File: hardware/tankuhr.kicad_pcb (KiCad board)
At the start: 2 copper layers, 50 x 50 mm, 30 parts, among them J1 Conn_01x04_Pin, J2 Conn_01x04_Pin, J3 Conn_01x04_Pin, U1 TBA1-1211, U2 XIAO-ESP32-C3-SMD

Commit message: start with r2 hardware
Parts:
- added D2: 1N5817, Diode_THT:D_DO-41_SOD81_P7.62mm_Horizontal, F.Cu at (59.0, 83.3)
- added D3: LED, LED_SMD:LED_PLCC-2_3.4x3.0mm_AK, F.Cu at (51.8, 71.2)
- added F1: 1A, Fuse:Fuse_1206_3216Metric, F.Cu at (55.5, 81.2)
- added JP1: SolderJumper_2_Bridged, Jumper:SolderJumper-2_P1.3mm_Bridged2Bar_Pad1.0x1.5mm, F.Cu at (95.8, 88.6)
- C3, C4, C5, C6, R6, R7: footprint Capacitor_SMD:C_0805_2012Metric -> Capacitor_SMD:C_0805_2012Metric_Pad1.18x1.45mm_HandSolder
- J1, J2, J3: footprint Connector_PinHeader_2.54mm:PinHeader_1x04_P2.54mm_Vertical -> Connector_JST:JST_GH_BM04B-GHS-TBT_1x04-1MP_P1.25mm_Vertical
- R1, R2, R3, R5: footprint Resistor_SMD:R_0805_2012Metric -> Resistor_SMD:R_0805_2012Metric_Pad1.20x1.40mm_HandSolder
- R4: value 0 -> ?; footprint Connector_PinHeader_2.54mm:PinHeader_1x02_P2.54mm_Vertical -> Resistor_SMD:R_0805_2012Metric_Pad1.20x1.40mm_HandSolder
- TP1, TP2, TP3, TP4: footprint TestPoint:TestPoint_THTPad_2.0x2.0mm_Drill1.0mm -> TestPoint:TestPoint_Pad_D1.0mm
- moved R4 39.6 mm to (56.6, 71.2)
- moved L1 4.94 mm to (61.9, 83.2)
- moved L2 4.94 mm to (61.9, 87.0)
- moved C2 4.69 mm to (81.2, 83.5)
- moved C3 4.69 mm to (74.8, 85.0)
- moved J1 3.98 mm to (50.8, 84.9), turned to 90 degrees
- moved J2 3.87 mm to (51.0, 63.1), turned to 90 degrees
- moved U1 3.69 mm to (91.7, 89.3)
- moved TP4 3.45 mm to (95.5, 81.8), turned to 0 degrees
- moved J3 2.85 mm to (94.0, 62.0), turned to -90 degrees
- moved TP1 2.54 mm to (56.0, 66.5)
- moved C5 1.83 mm to (58.9, 64.0)
- moved R5 1.83 mm to (58.9, 66.5)
- moved TP2 1.82 mm to (54.2, 57.8)
- moved C6 1.60 mm to (86.5, 57.5)
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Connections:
- C2 pad 2: Net-(U1--Vin) -> Net-(JP1-A)
- C3 pad 2: Net-(U1--Vin) -> Net-(JP1-A)
- J1 pad 1: +12V -> GNDA
- J1 pad 2: +12V -> GNDA
- J1 pad 3: GNDA -> Net-(J1-Pin_3)
- J1 pad 4: GNDA -> Net-(J1-Pin_3)
- J2 pad 1: SENSOR_FUEL_LEVEL -> SENSOR_FUEL_FLOW
- J2 pad 4: SENSOR_FUEL_FLOW -> SENSOR_FUEL_LEVEL
- L2 pad 2: Net-(U1--Vin) -> Net-(JP1-A)
- R4 pad 1: Net-(U1--Vin) -> USER_LED0
- R4 pad 2: GND -> Net-(D3-A)
- U1 pad 1: Net-(U1--Vin) -> Net-(JP1-A)
- U2 pad 4: unconnected-(U2-GPIO5_A3_D3-Pad4) -> USER_LED0
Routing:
- net Net-(U1--Vin): track 27.5 -> 0.00 mm
- net Net-(JP1-A): track 0.00 -> 26.0 mm
- net USER_LED0: track 0.00 -> 15.3 mm
- net GND: track 16.3 -> 29.0 mm, vias 15 -> 14
- net +12V: track 15.6 -> 2.99 mm
- net Net-(D2-A): track 0.00 -> 5.61 mm
- net GNDA: track 15.6 -> 10.5 mm
- net Net-(J3-Pin_1): track 33.5 -> 37.9 mm, vias 2 -> 0
- net +5V: track 4.30 -> 0.00 mm
- net Net-(J1-Pin_3): track 0.00 -> 4.14 mm
- net Net-(D3-A): track 0.00 -> 2.42 mm
- net SENSOR_FUEL_LEVEL: track 10.1 -> 8.44 mm
- net +3.3V: track 12.6 -> 11.0 mm
- net Net-(J3-Pin_4): track 33.4 -> 35.0 mm, vias 2 -> 0
- net Net-(U2-GPIO3_A1_D1): track 14.7 -> 16.2 mm
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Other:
- board text added: "Tankuhr r2"
- board text removed: "Tankuhr r1"

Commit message: WIP
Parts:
- removed D2: 1N5817, Diode_THT:D_DO-41_SOD81_P7.62mm_Horizontal
- removed D3: LED, LED_SMD:LED_PLCC-2_3.4x3.0mm_AK
- removed L2: 2uH, Inductor_THT:L_Axial_L7.0mm_D3.3mm_P10.16mm_Horizontal_Fastron_MICC
- removed R3: 390, Resistor_SMD:R_0805_2012Metric_Pad1.20x1.40mm_HandSolder
- removed R4: ?, Resistor_SMD:R_0805_2012Metric_Pad1.20x1.40mm_HandSolder
- added R10: 220, Resistor_SMD:R_0805_2012Metric_Pad1.20x1.40mm_HandSolder, F.Cu at (68.9, 103.8)
- added R11: 0, Resistor_SMD:R_0805_2012Metric_Pad1.20x1.40mm_HandSolder, F.Cu at (68.9, 106.8)
- added R8: 4.7k, Resistor_SMD:R_0805_2012Metric_Pad1.20x1.40mm_HandSolder, F.Cu at (83.0, 106.0)
- added R9: 100, Resistor_SMD:R_0805_2012Metric_Pad1.20x1.40mm_HandSolder, F.Cu at (68.9, 100.9)
- added U3: MCP6002-xMC, Package_DFN_QFN:DFN-8-1EP_3x2mm_P0.5mm_EP1.75x1.45mm, F.Cu at (74.0, 100.0)
- C1: value 22u / 10V -> 1n; footprint Capacitor_THT:CP_Radial_D4.0mm_P1.50mm -> Capacitor_SMD:C_0805_2012Metric_Pad1.18x1.45mm_HandSolder
- C2: value 100u / 35V -> 4.7u; footprint Capacitor_THT:CP_Radial_D8.0mm_P3.50mm -> Capacitor_THT:CP_Radial_D5.0mm_P2.00mm
- C3: value 100n / >35V -> 10u; footprint Capacitor_SMD:C_0805_2012Metric_Pad1.18x1.45mm_HandSolder -> Capacitor_THT:CP_Radial_D5.0mm_P2.00mm
- C5: value 100n -> 1n
- D1: value LED -> BAT54W; footprint LED_SMD:LED_PLCC-2_3.4x3.0mm_AK -> Package_TO_SOT_SMD:SOT-323_SC-70
- L1: value 2uH -> L; footprint Inductor_THT:L_Axial_L7.0mm_D3.3mm_P10.16mm_Horizontal_Fastron_MICC -> asdf:RECOM RLS-126
- R1: value 220 -> 3.3k / 330
- R2: value 6.8k -> 1k
- R5: value 330 -> 220
- R6, R7: footprint Capacitor_SMD:C_0805_2012Metric_Pad1.18x1.45mm_HandSolder -> Resistor_SMD:R_0805_2012Metric_Pad1.20x1.40mm_HandSolder
- U1: value TBA1-1211 -> R-78E5.0-0.5; footprint Converter_DCDC:Converter_DCDC_TRACO_TBA1-xxxx_THT -> Converter_DCDC:Converter_DCDC_RECOM_R-78E-0.5_THT
- moved U2 50.5 mm to (123.0, 59.6)
- moved D1 43.9 mm to (57.0, 81.3), turned to 0 degrees
- moved U1 15.9 mm to (77.3, 82.6), turned to -90 degrees
- moved C3 14.3 mm to (60.5, 86.0)
- moved C2 12.0 mm to (69.5, 86.0)
- moved TP4 9.74 mm to (87.0, 86.5)
- moved JP1 8.95 mm to (86.8, 89.5), turned to 0 degrees
- moved TP2 4.43 mm to (50.0, 56.5)
- moved TP1 3.91 mm to (53.0, 69.0)
- moved F1 3.58 mm to (54.0, 78.0), turned to 0 degrees
- moved L1 2.15 mm to (62.0, 81.0)
- moved R1 1.17 mm to (54.0, 56.0)
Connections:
- net Net-(J3-Pin_1) renamed SDA
- net Net-(J3-Pin_4) renamed SCL
- net Net-(U2-GPIO3_A1_D1) renamed D1
- C1 pad 1: Net-(U2-GPIO2_A0_D0) -> D0
- C2 pad 1: Net-(U1-+Vin) -> Net-(U1-IN)
- C2 pad 2: Net-(JP1-A) -> GNDA
- C3 pad 1: Net-(U1-+Vin) -> +12V
- C3 pad 2: Net-(JP1-A) -> GNDA
- D1 pad 1: GND -> Net-(D1-A)
- D1 pad 2: Net-(D1-A) -> unconnected-(D1-NC-Pad2)
- F1 pad 2: Net-(D2-A) -> Net-(D1-A)
- J3 pad 2: GND -> +3.3V
- JP1 pad 1: Net-(JP1-A) -> GNDA
- L1 pad 2: Net-(U1-+Vin) -> Net-(U1-IN)
- R1 pad 2: +5V -> +3.3V
- R2 pad 1: SENSOR_FUEL_LEVEL -> Net-(R10-Pad1)
- R2 pad 2: Net-(U2-GPIO2_A0_D0) -> Net-(U3A--)
- U1 pad 1: Net-(JP1-A) -> Net-(U1-IN)
- U1 pad 2: Net-(U1-+Vin) -> GNDA
- U1 pad 3: GND -> +5V
- U2 pad 1: Net-(U2-GPIO2_A0_D0) -> D0
- U2 pad 4: USER_LED0 -> unconnected-(U2-GPIO5_A3_D3-Pad4)
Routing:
- net SDA: track 37.9 -> 0.00 mm
- net SCL: track 35.0 -> 0.00 mm
- net GND: track 29.0 -> 0.00 mm, vias 14 -> 0
- net Net-(JP1-A): track 26.0 -> 0.00 mm
- net Net-(U1-+Vin): track 21.6 -> 0.00 mm
- net D1: track 16.2 -> 0.00 mm
- net USER_LED0: track 15.3 -> 0.00 mm
- net +3.3V: track 11.0 -> 0.00 mm
- net GNDA: track 10.5 -> 0.00 mm
- net Net-(U2-GPIO2_A0_D0): track 9.41 -> 0.00 mm
- net SENSOR_FUEL_LEVEL: track 8.44 -> 0.00 mm
- net SENSOR_FUEL_FLOW: track 5.67 -> 0.00 mm
- net Net-(D2-A): track 5.61 -> 0.00 mm
- net Net-(J1-Pin_3): track 4.14 -> 0.00 mm
- net Net-(D1-A): track 3.13 -> 0.00 mm
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- removed copper zone on F.Cu, net +5V
- removed copper zone on B.Cu, net GND
- removed copper zone on F.Cu, net GND

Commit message: complete r2 hardware
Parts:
- removed U3: MCP6002-xMC, Package_DFN_QFN:DFN-8-1EP_3x2mm_P0.5mm_EP1.75x1.45mm
- added D2: LED, LED_SMD:LED_0805_2012Metric_Pad1.15x1.40mm_HandSolder, F.Cu at (70.5, 71.5)
- added D3: LED, LED_SMD:LED_0805_2012Metric_Pad1.15x1.40mm_HandSolder, F.Cu at (73.0, 71.5)
- added D4: LED, LED_SMD:LED_0805_2012Metric_Pad1.15x1.40mm_HandSolder, F.Cu at (68.0, 71.5)
- added J4: Micro_SD_Card_Det1, Connector_Card:microSD_HC_Molex_104031-0811, F.Cu at (90.5, 65.1)
- added R12: 150, Resistor_SMD:R_0805_2012Metric_Pad1.20x1.40mm_HandSolder, F.Cu at (68.0, 75.5)
- added R3: 150, Resistor_SMD:R_0805_2012Metric_Pad1.20x1.40mm_HandSolder, F.Cu at (70.5, 75.5)
- added R4: 150, Resistor_SMD:R_0805_2012Metric_Pad1.20x1.40mm_HandSolder, F.Cu at (73.0, 75.5)
- added U5: MCP6001-OT, Package_TO_SOT_SMD:SOT-23-5, F.Cu at (57.5, 63.1)
- L1: footprint asdf:RECOM RLS-126 -> Library:RECOM RLS-120
- moved R10 49.2 mm to (59.5, 55.5), turned to 90 degrees
- moved U2 49.0 mm to (74.0, 58.5)
- moved R11 48.9 mm to (58.5, 59.0)
- moved R8 46.7 mm to (56.5, 67.5), turned to 90 degrees
- moved R9 39.0 mm to (62.9, 62.3), turned to -90 degrees
- moved TP3 25.8 mm to (90.0, 53.5)
- moved R7 18.2 mm to (89.0, 81.5), turned to -90 degrees
- moved R6 17.2 mm to (89.0, 77.5), turned to 90 degrees
- moved J3 16.8 mm to (93.6, 78.8)
- moved JP1 13.4 mm to (73.5, 89.7), turned to -90 degrees
- moved TP4 12.1 mm to (76.5, 92.5)
- moved R2 7.33 mm to (60.2, 62.5), turned to -90 degrees
- moved C5 4.38 mm to (61.5, 67.5), turned to 90 degrees
- moved D1 4.02 mm to (61.0, 81.0)
- moved C1 4.01 mm to (63.0, 52.5), turned to -90 degrees
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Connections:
- U2 pad 10: unconnected-(U2-GPIO9_D9_MISO-Pad10) -> /SD_MISO
- U2 pad 11: unconnected-(U2-GPIO10_D10_MOSI-Pad11) -> /SD_MOSI
- U2 pad 4: unconnected-(U2-GPIO5_A3_D3-Pad4) -> /LED_0
- U2 pad 7: unconnected-(U2-GPIO21_D6_TX-Pad7) -> /LED_1
- U2 pad 8: unconnected-(U2-GPIO20_D7_RX-Pad8) -> /SD_CS
- U2 pad 9: unconnected-(U2-GPIO8_D8_SCK-Pad9) -> /SD_CLK
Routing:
- net +5V: track 0.00 -> 48.3 mm, vias 0 -> 1
- net SCL: track 0.00 -> 34.3 mm
- net SDA: track 0.00 -> 32.2 mm
- net GNDA: track 0.00 -> 30.3 mm
- net +3.3V: track 0.00 -> 28.4 mm, vias 0 -> 12
- net D1: track 0.00 -> 20.0 mm
- net GND: track 0.00 -> 18.0 mm, vias 0 -> 22
- net /LED_0: track 0.00 -> 17.3 mm, vias 0 -> 2
- net /SD_MISO: track 0.00 -> 16.9 mm
- net /SD_MOSI: track 0.00 -> 16.2 mm
- net /SD_CS: track 0.00 -> 15.1 mm, vias 0 -> 2
- net /SD_CLK: track 0.00 -> 15.0 mm, vias 0 -> 2
- net Net-(U1-IN): track 0.00 -> 14.7 mm
- net SENSOR_FUEL_LEVEL: track 0.00 -> 13.7 mm
- net SENSOR_FUEL_FLOW: track 0.00 -> 10.2 mm
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- added copper zone on In2.Cu, net +3.3V
- added copper zone on B.Cu, net GND
- added copper zone on F.Cu, net GND
- added copper zone on In1.Cu, net GND
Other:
- copper layers 2 -> 4
- board text removed: "5V"

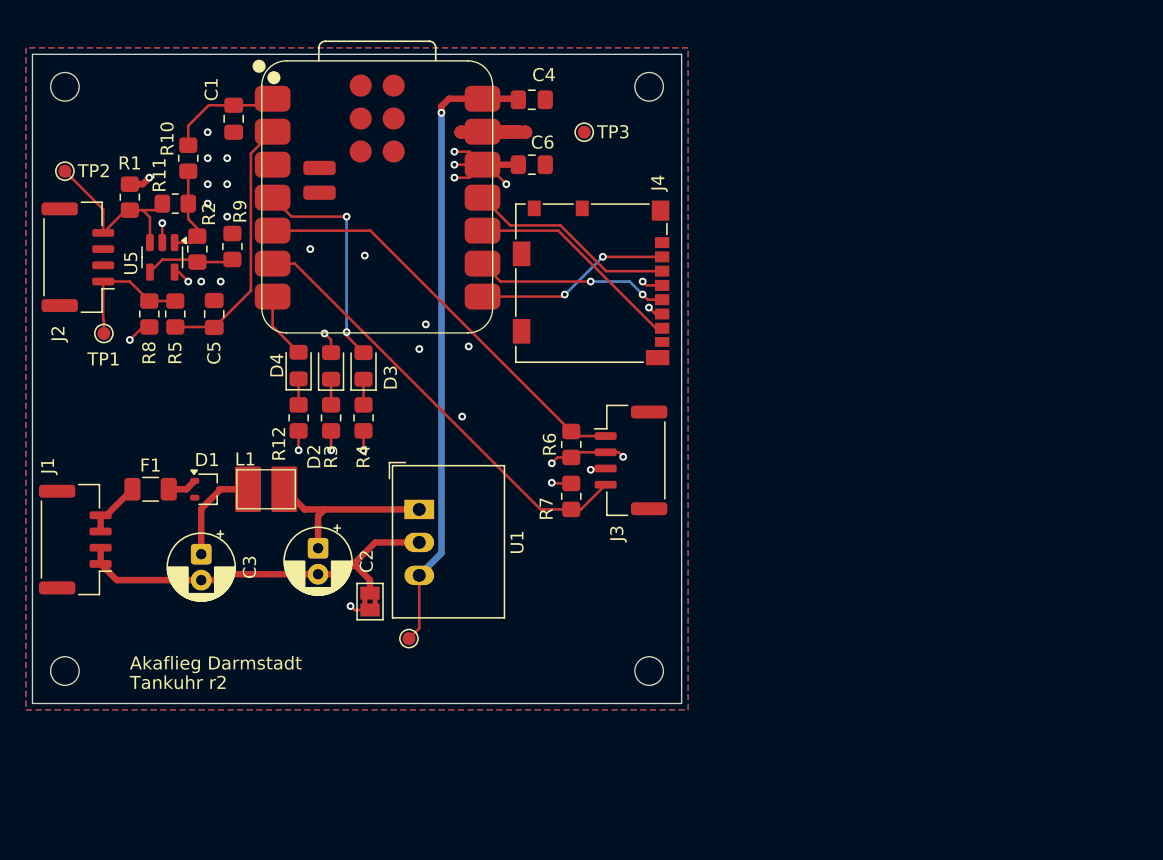
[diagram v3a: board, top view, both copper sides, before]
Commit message: hardware: new filter design
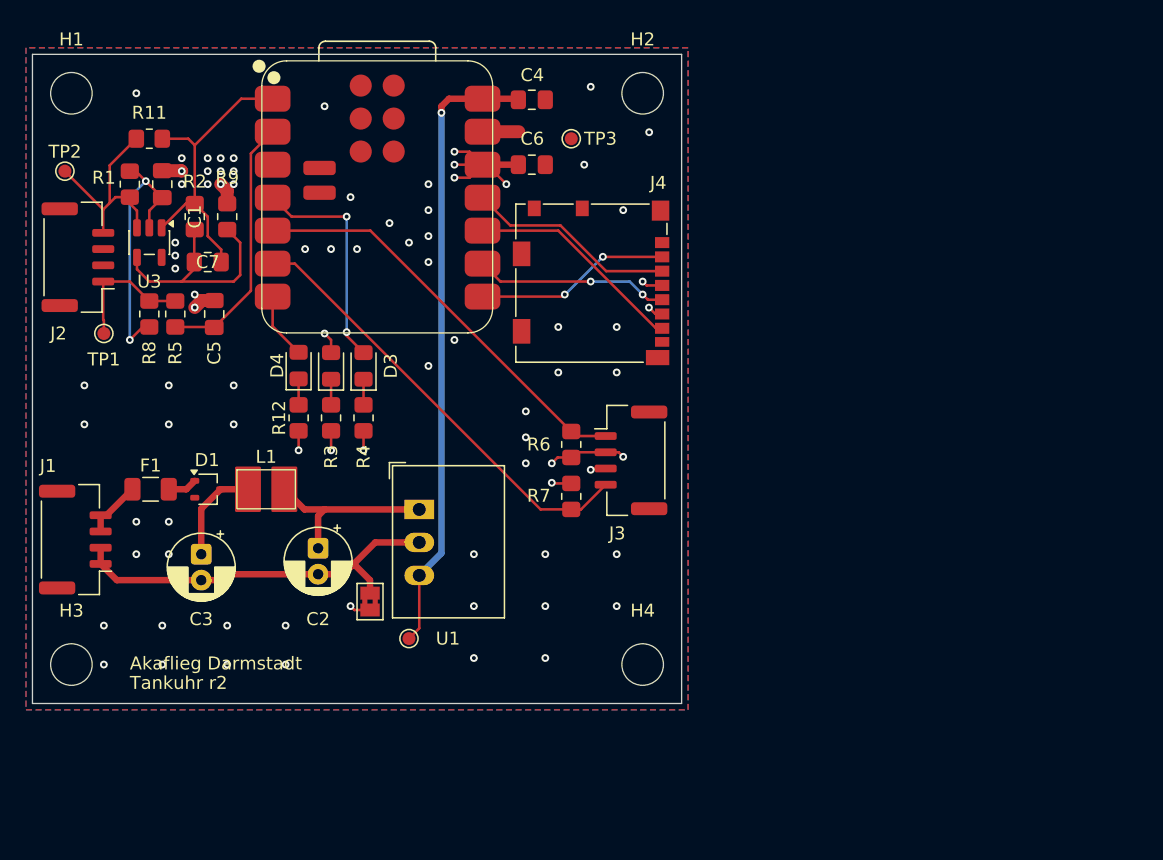
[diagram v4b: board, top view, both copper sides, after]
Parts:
- removed R10: 220, Resistor_SMD:R_0805_2012Metric_Pad1.20x1.40mm_HandSolder
- removed U5: MCP6001-OT, Package_TO_SOT_SMD:SOT-23-5
- added C7: 100n, Capacitor_SMD:C_0805_2012Metric_Pad1.18x1.45mm_HandSolder, F.Cu at (61.0, 63.5)
- added U3: MCP6001R, Package_TO_SOT_SMD:SOT-23-5, F.Cu at (56.5, 62.0)
- C1: value 1n -> 100n / >35V
- H1, H2, H3, H4: footprint MountingHole:MountingHole_2.2mm_M2 -> MountingHole:MountingHole_3.2mm_M3
- R2: value 1k -> 10k
- R9: value 100 -> 1k
- moved C1 7.46 mm to (57.5, 57.5), turned to 90 degrees
- moved R11 5.39 mm to (56.5, 54.0)
- moved R2 2.51 mm to (60.0, 60.0)
- moved R9 2.33 mm to (62.5, 60.0)
- moved TP3 1.12 mm to (89.0, 54.0)
- moved R1 1.00 mm to (55.0, 57.5)
- moved H1 0.71 mm to (50.5, 50.5)
- moved H2 0.71 mm to (94.5, 50.5)
- moved H3 0.71 mm to (50.5, 94.5)
- moved H4 0.71 mm to (94.5, 94.5)
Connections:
- C1 pad 1: D0 -> +3.3V
- R11 pad 2: Net-(R10-Pad1) -> D0
- R2 pad 1: Net-(R10-Pad1) -> D0
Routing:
- net +3.3V: track 28.4 -> 44.2 mm, vias 12 -> 11
- net D0: track 8.86 -> 24.1 mm
- net Net-(U3--): track 6.43 -> 17.8 mm
- net Net-(R10-Pad1): track 7.25 -> 0.00 mm
- net SENSOR_FUEL_LEVEL: track 13.7 -> 16.8 mm
- net GND: track 18.0 -> 16.3 mm, vias 22 -> 74

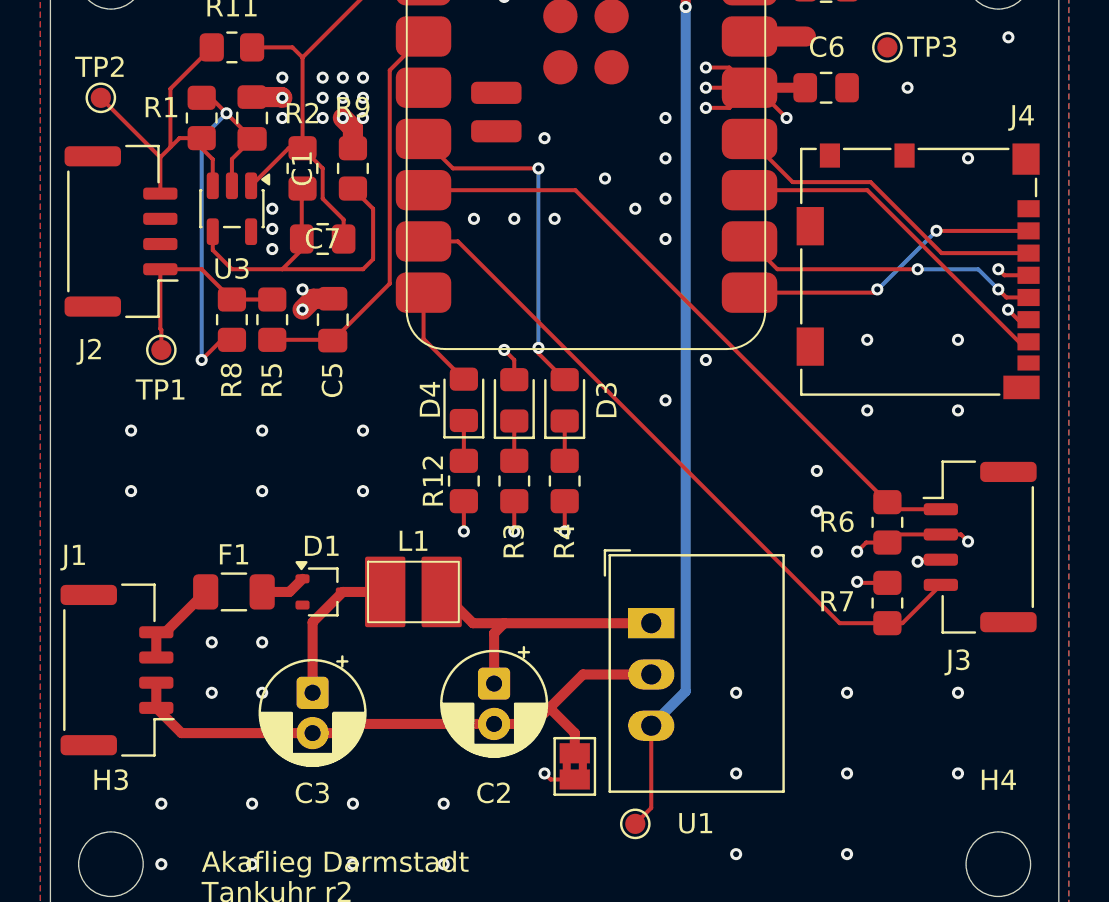
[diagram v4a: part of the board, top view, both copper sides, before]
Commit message: hardware: start BOM in kicad
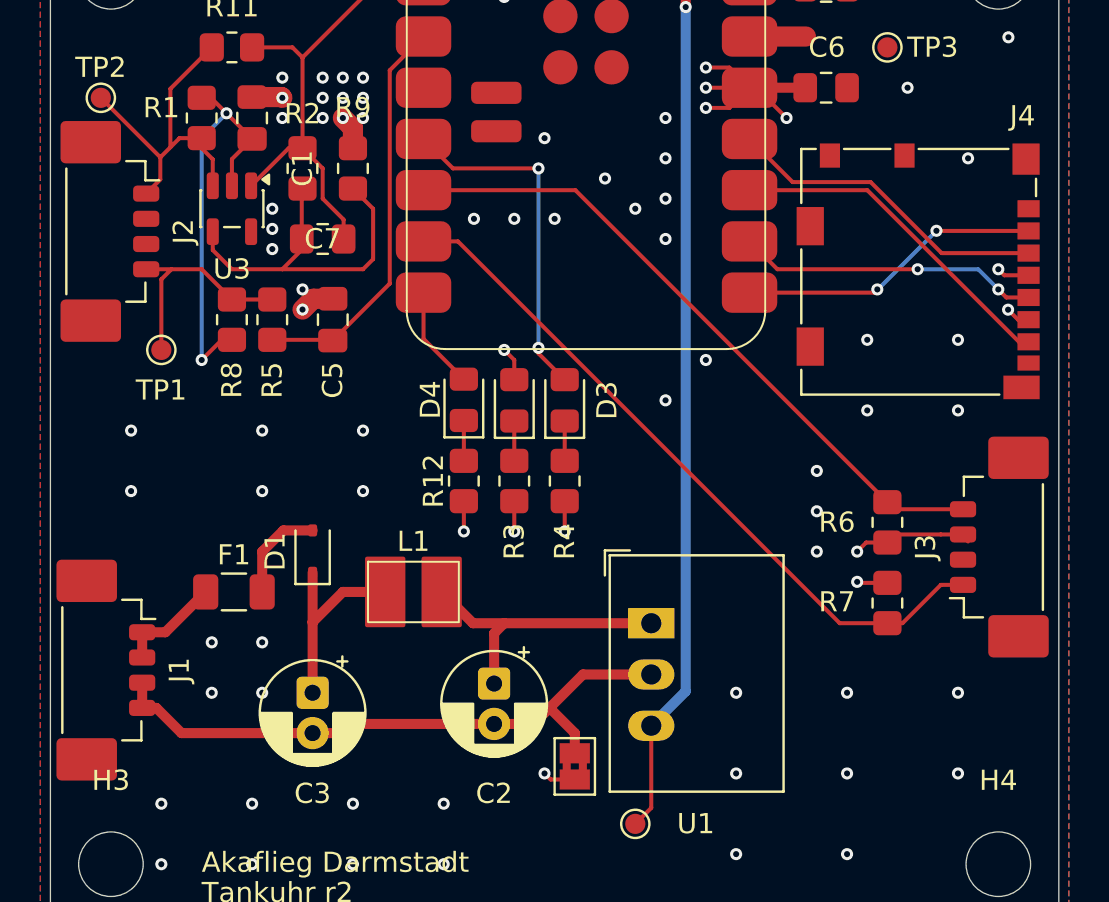
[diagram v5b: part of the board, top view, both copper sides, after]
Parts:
- C1, C4, C6: value 100n / >35V -> 100n
- D1: value BAT54W -> 1N5819WS; footprint Package_TO_SOT_SMD:SOT-323_SC-70 -> Diode_SMD:D_SOD-323
- J1, J2, J3: footprint Connector_JST:JST_GH_BM04B-GHS-TBT_1x04-1MP_P1.25mm_Vertical -> Connector_Molex:Molex_PicoBlade_53398-0471_1x04-1MP_P1.25mm_Vertical
- moved D1 2.06 mm to (60.5, 79.0), turned to 90 degrees
- moved J3 0.40 mm to (94.0, 78.8), turned to 90 degrees
- turned J1 to -90 degrees
- turned J2 to -90 degrees
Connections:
- D1 pad 1: Net-(D1-A) -> +12V
- D1 pad 2: unconnected-(D1-NC-Pad2) -> Net-(D1-A)
- F1 pad 1: Net-(J1-Pin_3) -> Net-(J1-Pin_1)
- J1 pad 1: GNDA -> Net-(J1-Pin_1)
- J1 pad 2: GNDA -> Net-(J1-Pin_1)
- J1 pad 3: Net-(J1-Pin_3) -> GNDA
- J1 pad 4: Net-(J1-Pin_3) -> GNDA
- J2 pad 1: SENSOR_FUEL_FLOW -> SENSOR_FUEL_LEVEL
- J2 pad 4: SENSOR_FUEL_LEVEL -> SENSOR_FUEL_FLOW
- J3 pad 1: SDA -> SCL
- J3 pad 2: +3.3V -> GND
- J3 pad 3: GND -> +3.3V
- J3 pad 4: SCL -> SDA
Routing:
- net Net-(J1-Pin_1): track 0.00 -> 5.23 mm
- net Net-(J1-Pin_3): track 4.53 -> 0.00 mm
- net Net-(D1-A): track 2.27 -> 4.93 mm
- net +12V: track 7.72 -> 10.2 mm
- net GND: track 16.3 -> 15.1 mm, vias 74 -> 73
- net SDA: track 32.2 -> 33.3 mm
- net SCL: track 34.3 -> 35.4 mm
- net SENSOR_FUEL_FLOW: track 10.2 -> 11.1 mm
- net GNDA: track 30.3 -> 31.0 mm
- net +3.3V: vias 11 -> 10
